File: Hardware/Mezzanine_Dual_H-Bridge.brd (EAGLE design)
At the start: 30.5 x 44.5 mm, 19 parts, among them U1 TB6612FNG, U2 EDISON_CONNECTOR_FULLMOUNTING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, U3 EDISON_CONNECTOR_FULLHEADER

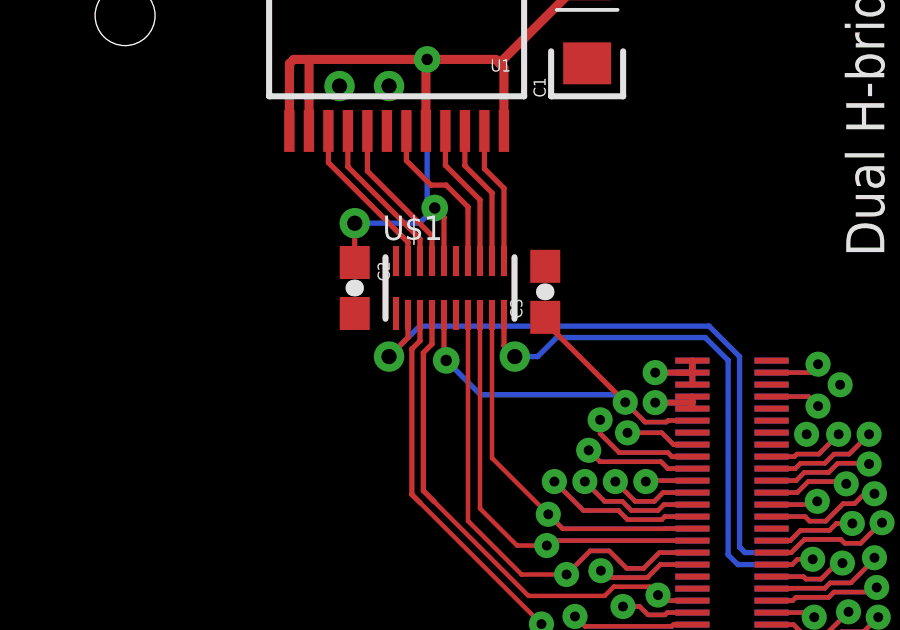
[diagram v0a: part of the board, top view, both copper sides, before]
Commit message: fixed OE high
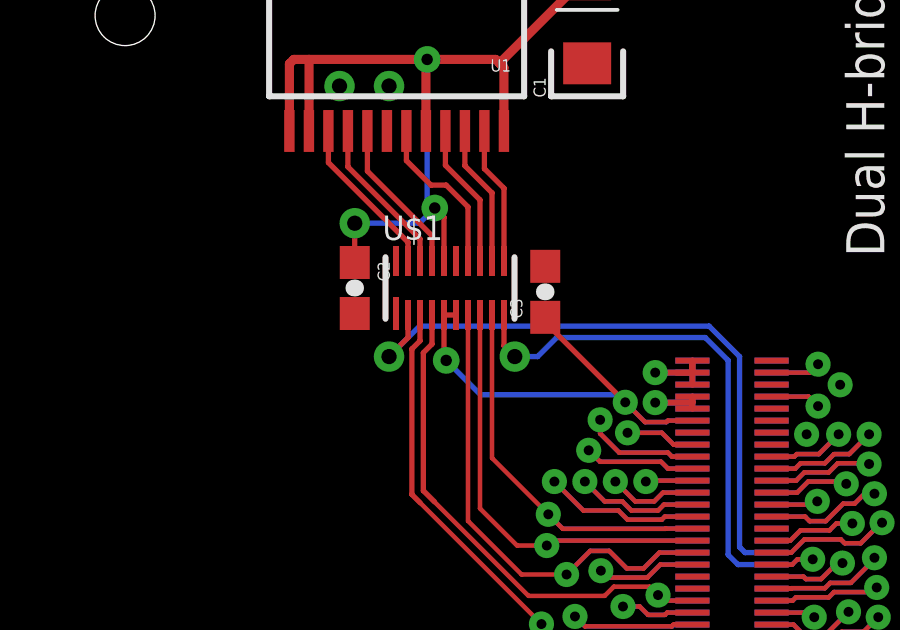
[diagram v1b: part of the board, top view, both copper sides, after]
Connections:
- net 1.8V: now also U$1.P$6
- net GND: no longer U$1.P$6
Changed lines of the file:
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@@
 <contactref element="U1" pad="18"/>
 <contactref element="U$1" pad="P$15"/>
-<contactref element="U$1" pad="P$6"/>
 <via x="13.208" y="32.131" extent="1-16" drill="0.508"/>
 <via x="11.557" y="32.131" extent="1-16" drill="0.508"/>
@@
 <wire x1="18.415" y1="24.423" x2="18.415" y2="24.257" width="0.1778" layer="1"/>
 <wire x1="18.415" y1="24.257" x2="21.082" y2="21.59" width="0.1778" layer="1"/>
+<contactref element="U$1" pad="P$6"/>
+<wire x1="15.04" y1="24.5" x2="15.44" y2="24.5" width="0.1778" layer="1"/>
 </signal>
 <signal name="FW_RCVR">

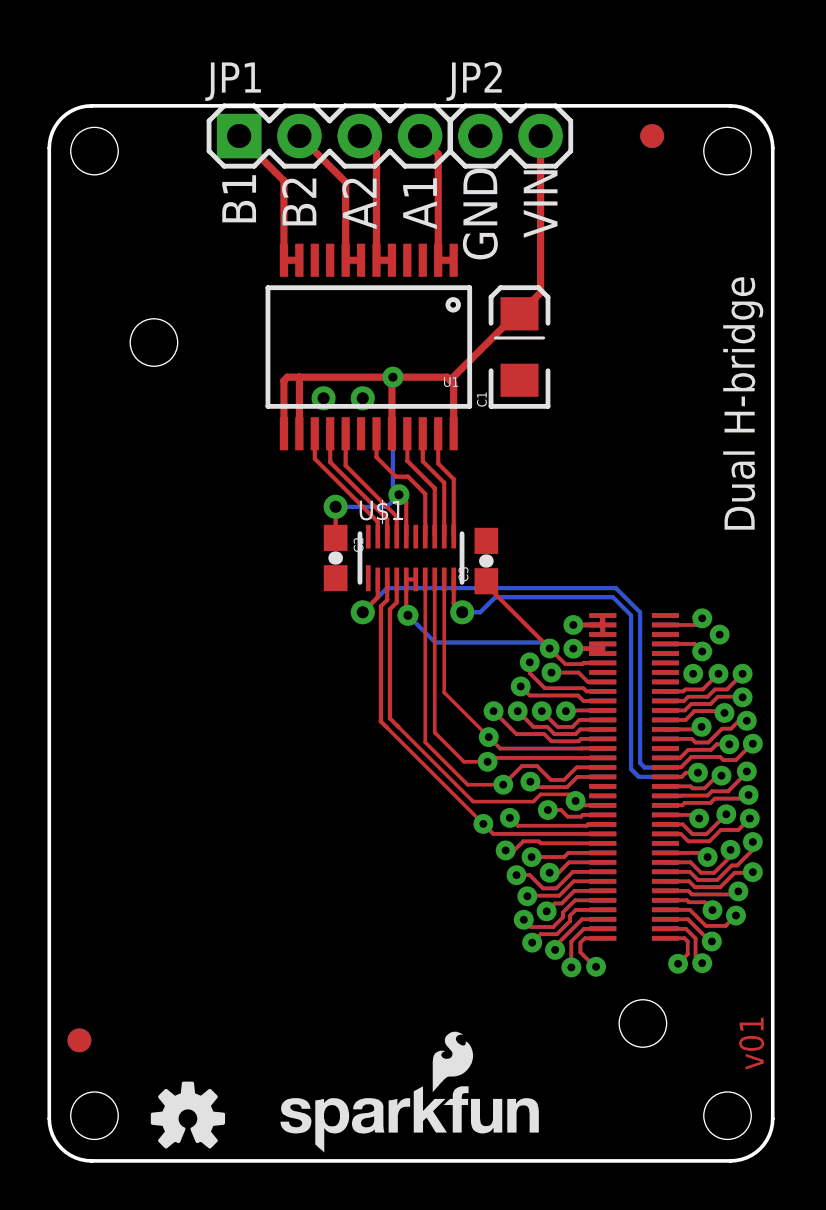
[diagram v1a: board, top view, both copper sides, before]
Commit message: Added LED's for motor direction Added Diode Jumper circuit to enable VSYS to power VIN Corrected Name and location Removed extra dimensions and cleaned up drawing Added DCIN pin and completed circuit.
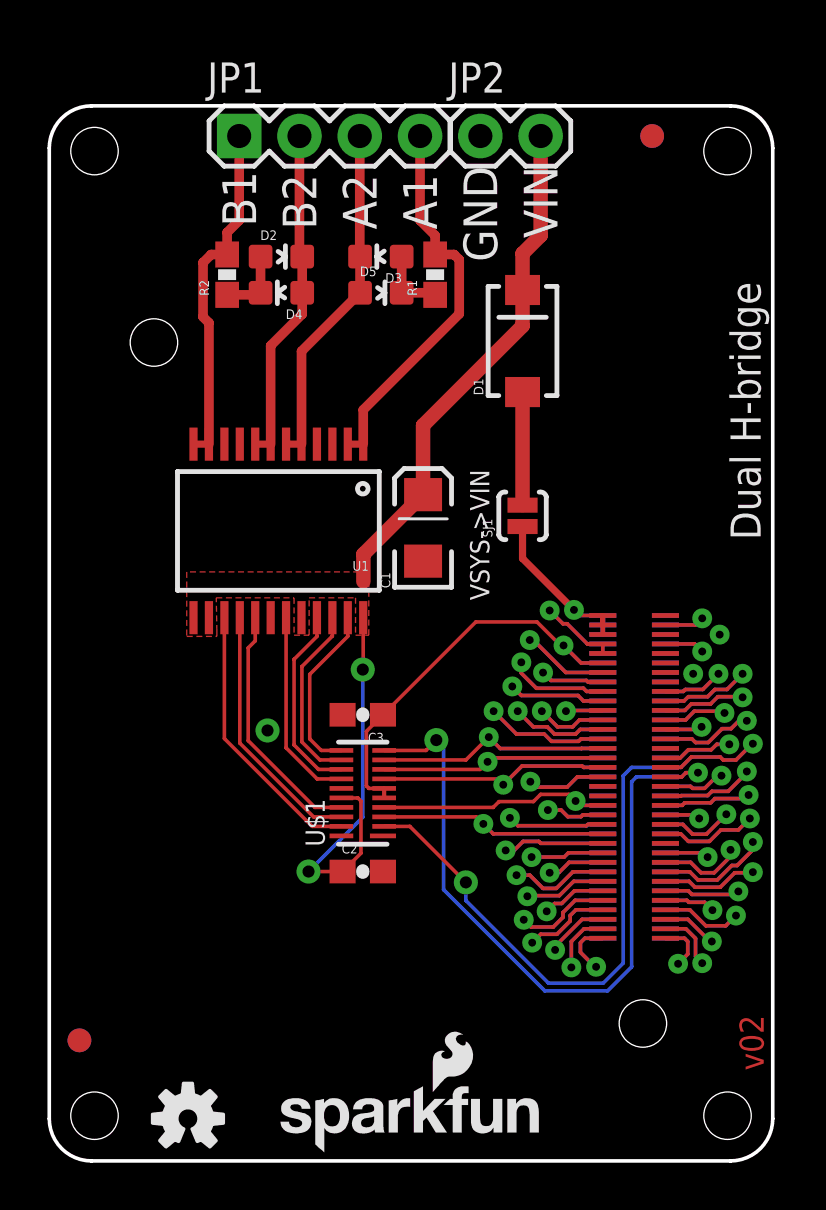
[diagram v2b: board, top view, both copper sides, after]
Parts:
- added D1: MBRA140, SparkFun-DiscreteSemi:SMA-DIODE
- added D2, D3: GREEN, SparkFun-LED:LED-0603
- added D4, D5: RED, SparkFun-LED:LED-0603
- added R1, R2: 2.0k, SparkFun-Resistors:0603-RES
- added SJ1: VSYS ENABLE, SparkFun-Passives:PAD-JUMPER-2-NO_YES_SILK
- moved C2 13.3 mm to (13.2, 12.2), turned to 0 degrees
- moved U$1 10.1 mm to (13.2, 15.5), turned to 90 degrees
- moved C1 8.64 mm to (15.7, 26.7)
- moved U1 8.63 mm to (9.65, 26.5)
- moved C3 8.31 mm to (13.2, 18.8), turned to 180 degrees
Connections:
- new net DCIN: U2.14, U3.14
- new net N$1: D1.A, SJ1.2
- new net N$2: D2.A, D4.C, R2.1
- new net N$5: D3.A, D5.C, R1.1
- net A1: now also R1.2
- net A2: now also D3.C, D5.A
- net B1: now also R2.2
- net B2: now also D2.C, D4.A
- net VIN: now also D1.C
- net VSYS: now also SJ1.1
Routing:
- net GP12_PWM0: track 20.2 -> 31.1 mm
- net A1: track 6.20 -> 16.5 mm
- net A2: track 6.18 -> 14.7 mm
- net B1: track 6.67 -> 14.8 mm
- net GP14: track 22.6 -> 14.7 mm
- net B2: track 6.69 -> 14.2 mm
- net DCIN: track 0.00 -> 7.28 mm, vias 0 -> 1
- net GP15: track 18.0 -> 10.9 mm
- net GP49: track 20.8 -> 14.2 mm
- net N$3: track 5.43 -> 11.6 mm
- net N$12: track 5.33 -> 10.9 mm
- net N$11: track 5.23 -> 10.4 mm
- net N$1: track 0.00 -> 4.77 mm
- net GP48: track 19.0 -> 14.3 mm
- net VSYS: track 4.48 -> 9.03 mm
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- added copper zone on layer 1, net VIN
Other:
- board text added: "Note: Units are in Inches"
- board text added: "VSYS->VIN"
- board text added: "v02"
- board text removed: "Connectors Go Here"
- board text removed: "LED's and selector switches go here"
- board text removed: "Max Board Length"
- board text removed: "Nothing goes here... I mean it."
- board text removed: "v01"

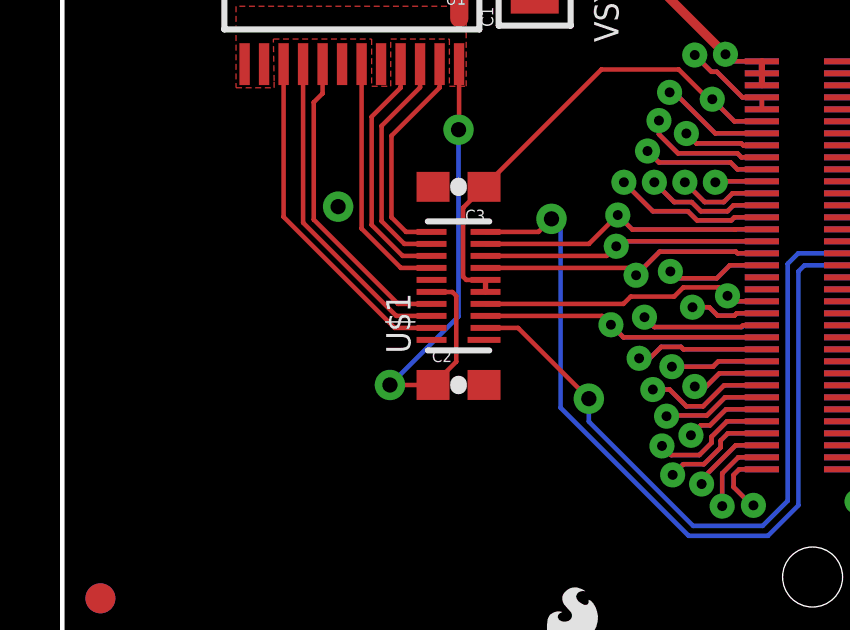
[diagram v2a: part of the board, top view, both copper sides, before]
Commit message: corrected labels
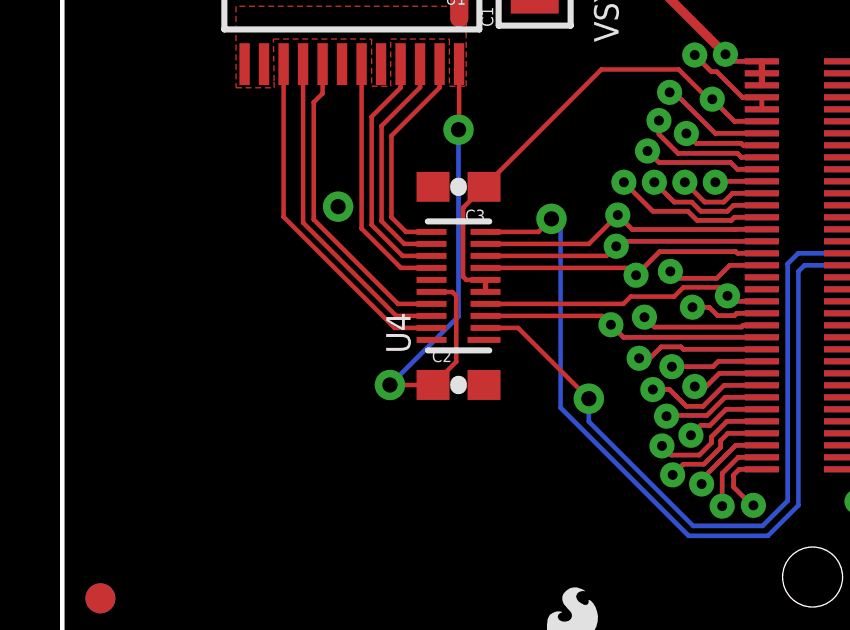
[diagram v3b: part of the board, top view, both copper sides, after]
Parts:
- renumbered U$1 to U4
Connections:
- net 1.8V: now also U4.5, U4.6; no longer U4.P$5, U4.P$6
- net GND: now also U4.15; no longer U4.P$15
- net GP12_PWM0: now also U4.10; no longer U4.P$10
- net GP13_PWM1: now also U4.2; no longer U4.P$2
- net GP14: now also U4.3; no longer U4.P$3
- net GP15: now also U4.4; no longer U4.P$4
- net GP47: now also U4.9; no longer U4.P$9
- net GP48: now also U4.8; no longer U4.P$8
- net GP49: now also U4.7; no longer U4.P$7
- net N$10: now also U4.14; no longer U4.P$14
- net N$11: now also U4.17; no longer U4.P$17
- net N$12: now also U4.18; no longer U4.P$18
- net N$14: now also U4.13; no longer U4.P$13
- net N$15: now also U4.12; no longer U4.P$12
- net N$3: now also U4.19; no longer U4.P$19
- net N$4: now also U4.11; no longer U4.P$11
- net VIN: now also U4.16; no longer U4.P$16
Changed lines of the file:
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@@
 <element name="JP1" library="SparkFun-Connectors" package="1X04" value="" x="8.001" y="43.18"/>
 <element name="JP2" library="SparkFun-Connectors" package="1X02" value="M02PTH" x="18.161" y="43.18"/>
-<element name="U$1" library="Testing" package="UFDFN-20" value="TXB0108" x="13.208" y="15.494" rot="R90"/>
+<element name="U4" library="Testing" package="UFDFN-20" value="TXB0108" x="13.208" y="15.494" rot="R90">
+<attribute name="PROD_ID" value="IC-12292" x="13.208" y="15.494" size="1.778" layer="27" rot="R90" display="off"/>
+</element>
 <element name="C1" library="SparkFun-Capacitors" package="EIA3216" value="10uF" x="15.748" y="26.67" rot="R90">
 <attribute name="PROD_ID" value="CAP-00811" x="15.748" y="26.67" size="1.778" layer="27" rot="R90" display="off"/>
@@
 <contactref element="U1" pad="3"/>
 <contactref element="U1" pad="18"/>
-<contactref element="U$1" pad="P$15"/>
+<contactref element="U4" pad="15"/>
 <contactref element="C3" pad="2"/>
 <contactref element="C1" pad="C"/>
@@
 <contactref element="U2" pad="33"/>
 <contactref element="U3" pad="33"/>
-<contactref element="U$1" pad="P$2"/>
+<contactref element="U4" pad="2"/>
 <wire x1="25.96" y1="16.58" x2="24.5302" y2="16.58" width="0.1524" layer="16"/>
 <wire x1="24.5302" y1="16.58" x2="24.1808" y2="16.2306" width="0.1524" layer="16"/>
@@
 <contactref element="U2" pad="35"/>
 <contactref element="U3" pad="35"/>
-<contactref element="U$1" pad="P$10"/>
+<contactref element="U4" pad="10"/>
 <wire x1="25.96" y1="16.18" x2="24.7398" y2="16.18" width="0.1524" layer="16"/>
 <wire x1="24.7398" y1="16.18" x2="24.5364" y2="15.9766" width="0.1524" layer="16"/>
@@
 <contactref element="U2" pad="48"/>
 <contactref element="U3" pad="48"/>
-<contactref element="U$1" pad="P$3"/>
+<contactref element="U4" pad="3"/>
 <wire x1="23.32" y1="13.7798" x2="18.7068" y2="13.7798" width="0.1524" layer="1"/>
 <wire x1="18.7068" y1="13.7798" x2="18.288" y2="14.1986" width="0.1524" layer="1"/>
@@
 <contactref element="U2" pad="42"/>
 <contactref element="U3" pad="42"/>
-<contactref element="U$1" pad="P$4"/>
+<contactref element="U4" pad="4"/>
 <wire x1="22.1742" y1="15.1638" x2="21.8948" y2="15.4432" width="0.1524" layer="1"/>
 <wire x1="21.8948" y1="15.4432" x2="20.701" y2="15.4432" width="0.1524" layer="1"/>
@@
 <contactref element="U2" pad="34"/>
 <contactref element="U3" pad="34"/>
-<contactref element="U$1" pad="P$7"/>
+<contactref element="U4" pad="7"/>
 <wire x1="14.108" y1="16.094" x2="18.8818" y2="16.094" width="0.1524" layer="1"/>
 <wire x1="18.8818" y1="16.094" x2="19.1262" y2="15.8496" width="0.1524" layer="1"/>
@@
 <contactref element="U2" pad="32"/>
 <contactref element="U3" pad="32"/>
-<contactref element="U$1" pad="P$8"/>
+<contactref element="U4" pad="8"/>
 <wire x1="23.32" y1="16.9798" x2="18.6308" y2="16.9798" width="0.1524" layer="1"/>
 <wire x1="18.6308" y1="16.9798" x2="18.4658" y2="16.8148" width="0.1524" layer="1"/>
@@
 <contactref element="U2" pad="30"/>
 <contactref element="U3" pad="30"/>
-<contactref element="U$1" pad="P$9"/>
+<contactref element="U4" pad="9"/>
 <wire x1="18.9992" y1="17.3736" x2="18.5166" y2="17.8562" width="0.1524" layer="16"/>
 <wire x1="18.9992" y1="17.3736" x2="18.5166" y2="17.8562" width="0.1524" layer="1"/>
@@
 <via x="21.6662" y="21.717" extent="1-16" drill="0.3302"/>
 <wire x1="23.3194" y1="20.9804" x2="23.32" y2="20.9798" width="0.1524" layer="1"/>
-<contactref element="U$1" pad="P$5"/>
+<contactref element="U4" pad="5"/>
 <contactref element="C3" pad="1"/>
-<contactref element="U$1" pad="P$6"/>
+<contactref element="U4" pad="6"/>
 <wire x1="14.108" y1="15.294" x2="14.108" y2="15.694" width="0.1778" layer="1"/>
 <wire x1="14.108" y1="15.694" x2="13.4652" y2="15.694" width="0.1524" layer="1"/>
@@
 <signal name="N$10">
 <contactref element="U1" pad="19"/>
-<contactref element="U$1" pad="P$14"/>
+<contactref element="U4" pad="14"/>
 <wire x1="9.977" y1="22.887" x2="9.977" y2="17.4042" width="0.1524" layer="1"/>
 <wire x1="9.977" y1="17.4042" x2="11.2872" y2="16.094" width="0.1524" layer="1"/>
@@
 <signal name="N$11">
 <contactref element="U1" pad="17"/>
-<contactref element="U$1" pad="P$17"/>
+<contactref element="U4" pad="17"/>
 <wire x1="8.382" y1="17.7038" x2="11.1918" y2="14.894" width="0.1524" layer="1"/>
 <wire x1="11.1918" y1="14.894" x2="12.308" y2="14.894" width="0.1524" layer="1"/>
@@
 <signal name="N$12">
 <contactref element="U1" pad="16"/>
-<contactref element="U$1" pad="P$18"/>
+<contactref element="U4" pad="18"/>
 <wire x1="12.308" y1="14.494" x2="11.1346" y2="14.494" width="0.1524" layer="1"/>
 <wire x1="11.1346" y1="14.494" x2="8.027" y2="17.6016" width="0.1524" layer="1"/>
@@
 <signal name="N$14">
 <contactref element="U1" pad="21"/>
-<contactref element="U$1" pad="P$13"/>
+<contactref element="U4" pad="13"/>
 <wire x1="11.277" y1="22.887" x2="11.277" y2="22.0974" width="0.1524" layer="1"/>
 <wire x1="11.277" y1="22.0974" x2="10.3124" y2="21.1328" width="0.1524" layer="1"/>
@@
 <signal name="N$15">
 <contactref element="U1" pad="22"/>
-<contactref element="U$1" pad="P$12"/>
+<contactref element="U4" pad="12"/>
 <wire x1="11.927" y1="22.887" x2="11.927" y2="22.1124" width="0.1524" layer="1"/>
 <wire x1="11.927" y1="22.1124" x2="10.6426" y2="20.828" width="0.1524" layer="1"/>
@@
 <contactref element="U1" pad="24"/>
 <contactref element="U1" pad="20"/>
-<contactref element="U$1" pad="P$16"/>
+<contactref element="U4" pad="16"/>
 <contactref element="C2" pad="1"/>
 <contactref element="C1" pad="A"/>
@@
 <signal name="N$3">
 <contactref element="U1" pad="15"/>
-<contactref element="U$1" pad="P$19"/>
+<contactref element="U4" pad="19"/>
 <wire x1="7.377" y1="22.887" x2="7.377" y2="17.7944" width="0.1524" layer="1"/>
 <wire x1="7.377" y1="17.7944" x2="11.0774" y2="14.094" width="0.1524" layer="1"/>
@@
 <signal name="N$4">
 <contactref element="U1" pad="23"/>
-<contactref element="U$1" pad="P$11"/>
+<contactref element="U4" pad="11"/>
 <wire x1="12.577" y1="22.887" x2="12.577" y2="22.102" width="0.1524" layer="1"/>
 <wire x1="12.577" y1="22.102" x2="10.9728" y2="20.4978" width="0.1524" layer="1"/>
